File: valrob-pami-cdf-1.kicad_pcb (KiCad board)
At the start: 4 copper layers, 58 x 50 mm, 138 parts, among them J1 Conn_01x04, J2 USB_C_Receptacle_USB2.0_14P, J3 Conn_01x02, J4 Conn_01x04_Pin, J5 Conn_01x06, M1 Motor_Servo, M2 Stepper_Motor_bipolar, M3 Stepper_Motor_bipolar, Q1 Q_NMOS, Q2 Q_NMOS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

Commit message: pcb: add RGB led routing
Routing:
- net /RGB1: track 0.00 -> 14.3 mm
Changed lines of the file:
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@@
+	)
+	(segment
+		(start 162.25 98)
+		(end 161.5 98.75)
+		(width 0.2)
+		(layer "F.Cu")
+		(net 37)
+	)
+	(segment
+		(start 161.5 98.75)
+		(end 158 98.75)
+		(width 0.2)
+		(layer "F.Cu")
+		(net 37)
+	)
+	(segment
+		(start 162.25 94.75)
+		(end 162.25 98)
+		(width 0.2)
+		(layer "F.Cu")
+		(net 37)
+	)
+	(segment
+		(start 164.8 91.7)
+		(end 164.531 91.969)
+		(width 0.2)
+		(layer "F.Cu")
+		(net 37)
+	)
+	(segment
+		(start 158 98.75)
+		(end 157.6 98.35)
+		(width 0.2)
+		(layer "F.Cu")
+		(net 37)
+	)
+	(segment
+		(start 164.531 92.469)
+		(end 162.25 94.75)
+		(width 0.2)
+		(layer "F.Cu")
+		(net 37)
+	)
+	(segment
+		(start 165.3 91.7)
+		(end 164.8 91.7)
+		(width 0.2)
+		(layer "F.Cu")
+		(net 37)
+	)
+	(segment
+		(start 157.6 98.35)
+		(end 157.6 97.05)
+		(width 0.2)
+		(layer "F.Cu")
+		(net 37)
+	)
+	(segment
+		(start 164.531 91.969)
+		(end 164.531 92.469)
+		(width 0.2)
+		(layer "F.Cu")
+		(net 37)
 	)
 	(segment
@@
 	)
 	(segment
-		(start 165.3 91.3)
-		(end 164.872936 91.3)
+		(start 164.01 91.75)
+		(end 164.25 91.51)
 		(width 0.2)
 		(layer "F.Cu")
@@
 	)
 	(segment
-		(start 164.422936 91.75)
-		(end 164.01 91.75)
+		(start 164.25 91.5)
+		(end 164.45 91.3)
 		(width 0.2)
 		(layer "F.Cu")
@@
 	)
 	(segment
-		(start 164.872936 91.3)
-		(end 164.422936 91.75)
-		(width 0.2)
-		(layer "F.Cu")
+		(start 164.25 91.51)
+		(end 164.25 91.5)
+		(width 0.2)
+		(layer "F.Cu")
+		(net 78)
+	)
+	(segment
+		(start 164.45 91.3)
+		(end 165.3 91.3)
+		(width 0.2)
+		(layer "F.Cu")

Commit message: pcb: add spare gpio routing
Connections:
- U4 pad 39: Net-(J5-Pin_2) -> Net-(J5-Pin_4)
- U4 pad 40: Net-(J5-Pin_3) -> Net-(J5-Pin_2)
- U4 pad 41: Net-(J5-Pin_4) -> Net-(J5-Pin_5)
- U4 pad 42: Net-(J5-Pin_5) -> Net-(J5-Pin_3)
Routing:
- net Net-(J5-Pin_2): track 0.00 -> 11.5 mm
- net Net-(J5-Pin_4): track 0.00 -> 9.92 mm, vias 0 -> 1
- net Net-(J5-Pin_3): track 0.00 -> 7.77 mm
- net Net-(J5-Pin_5): track 0.00 -> 5.07 mm
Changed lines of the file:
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@@
 			(layers "F.Cu" "F.Mask" "F.Paste")
 			(roundrect_rratio 0.25)
-			(net 118 "Net-(J5-Pin_2)")
+			(net 117 "Net-(J5-Pin_4)")
 			(pinfunction "GPIO34")
 			(pintype "bidirectional")
@@
 			(layers "F.Cu" "F.Mask" "F.Paste")
 			(roundrect_rratio 0.25)
-			(net 119 "Net-(J5-Pin_3)")
+			(net 118 "Net-(J5-Pin_2)")
 			(pinfunction "GPIO35")
 			(pintype "bidirectional")
@@
 			(layers "F.Cu" "F.Mask" "F.Paste")
 			(roundrect_rratio 0.25)
-			(net 117 "Net-(J5-Pin_4)")
+			(net 116 "Net-(J5-Pin_5)")
 			(pinfunction "GPIO36")
 			(pintype "bidirectional")
@@
 			(layers "F.Cu" "F.Mask" "F.Paste")
 			(roundrect_rratio 0.25)
-			(net 116 "Net-(J5-Pin_5)")
+			(net 119 "Net-(J5-Pin_3)")
 			(pinfunction "GPIO37")
 			(pintype "bidirectional")
@@
 	)
 	(segment
+		(start 169 97.21)
+		(end 169 96.5)
+		(width 0.2)
+		(layer "F.Cu")
+		(net 116)
+	)
+	(segment
+		(start 170.95 94.55)
+		(end 170.95 92.95)
+		(width 0.2)
+		(layer "F.Cu")
+		(net 116)
+	)
+	(segment
+		(start 169 96.5)
+		(end 170.95 94.55)
+		(width 0.2)
+		(layer "F.Cu")
+		(net 116)
+	)
+	(segment
+		(start 170.138088 92.938088)
+		(end 170.15 92.95)
+		(width 0.2)
+		(layer "F.Cu")
+		(net 117)
+	)
+	(segment
+		(start 170.138088 92.301707)
+		(end 170.138088 92.938088)
+		(width 0.2)
+		(layer "F.Cu")
+		(net 117)
+	)
+	(via
+		(at 170.138088 92.301707)
+		(size 0.5)
+		(drill 0.3)
+		(layers "F.Cu" "B.Cu")
+		(net 117)
+	)
+	(segment
+		(start 168.25 96)
+		(end 168.75 96)
+		(width 0.2)
+		(layer "B.Cu")
+		(net 117)
+	)
+	(segment
+		(start 170.138088 94.611912)
+		(end 170.138088 92.301707)
+		(width 0.2)
+		(layer "B.Cu")
+		(net 117)
+	)
+	(segment
+		(start 167.75 98.46)
+		(end 167.75 96.5)
+		(width 0.2)
+		(layer "B.Cu")
+		(net 117)
+	)
+	(segment
+		(start 166.46 99.75)
+		(end 167.75 98.46)
+		(width 0.2)
+		(layer "B.Cu")
+		(net 117)
+	)
+	(segment
+		(start 167.75 96.5)
+		(end 168.25 96)
+		(width 0.2)
+		(layer "B.Cu")
+		(net 117)
+	)
+	(segment
+		(start 168.75 96)
+		(end 170.138088 94.611912)
+		(width 0.2)
+		(layer "B.Cu")
+		(net 117)
+	)
+	(segment
+		(start 169.003612 96)
+		(end 170.55 94.453612)
+		(width 0.2)
+		(layer "F.Cu")
+		(net 118)
+	)
+	(segment
+		(start 166.46 102.29)
+		(end 167.75 101)
+		(width 0.2)
+		(layer "F.Cu")
+		(net 118)
+	)
+	(segment
+		(start 170.55 94.453612)
+		(end 170.55 92.95)
+		(width 0.2)
+		(layer "F.Cu")
+		(net 118)
+	)
+	(segment
+		(start 167.75 101)
+		(end 167.75 96.543479)
+		(width 0.2)
+		(layer "F.Cu")
+		(net 118)
+	)
+	(segment
+		(start 167.75 96.543479)
+		(end 168.293479 96)
+		(width 0.2)
+		(layer "F.Cu")
+		(net 118)
+	)
+	(segment
+		(start 168.293479 96)
+		(end 169.003612 96)
+		(width 0.2)
+		(layer "F.Cu")
+		(net 118)
+	)
+	(segment
+		(start 171.35 94.65)
+		(end 171.35 92.95)
+		(width 0.2)
+		(layer "F.Cu")
+		(net 119)
+	)
+	(segment
+		(start 170.101 95.899)
+		(end 171.35 94.65)
+		(width 0.2)
+		(layer "F.Cu")
+		(net 119)
+	)
+	(segment
+		(start 169 99.75)
+		(end 170.101 98.649)
+		(width 0.2)
+		(layer "F.Cu")
+		(net 119)
+	)
+	(segment
+		(start 170.101 98.649)
+		(end 170.101 95.899)
+		(width 0.2)
+		(layer "F.Cu")
+		(net 119)
+	)
+	(segment

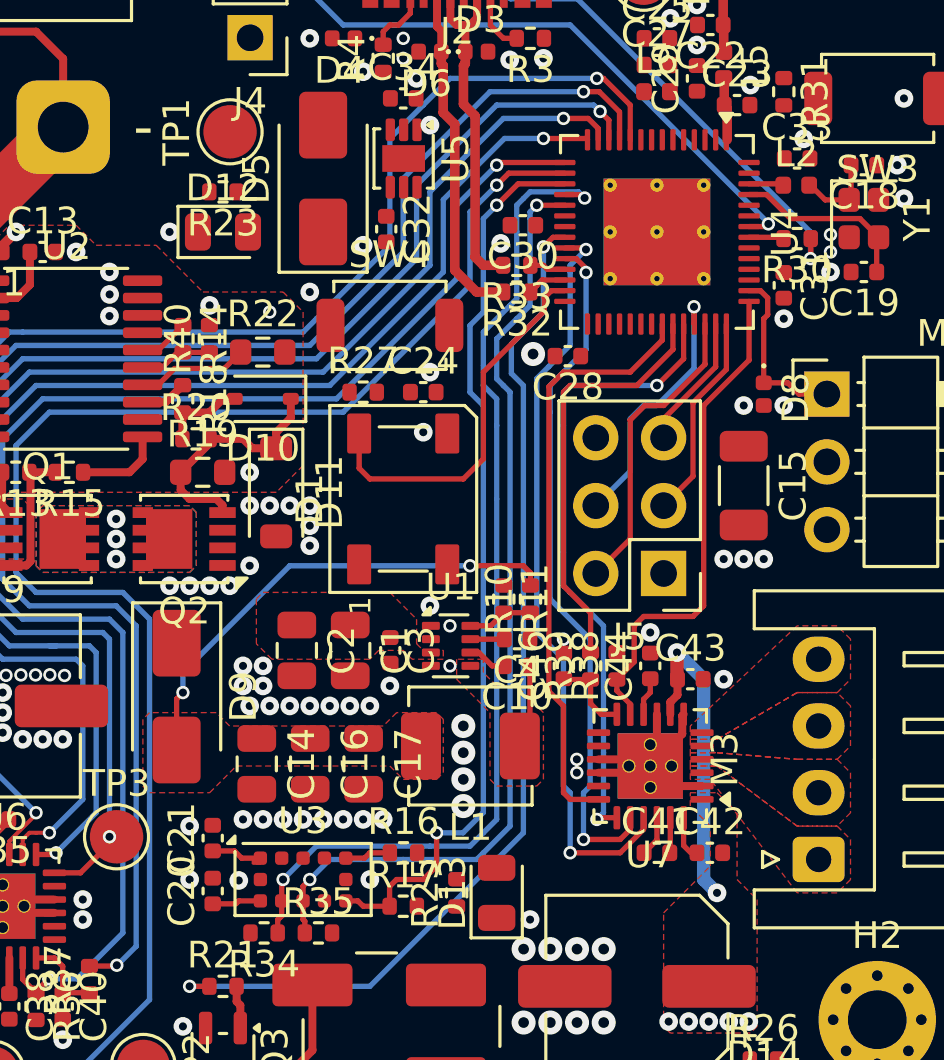
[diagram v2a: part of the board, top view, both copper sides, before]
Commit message: pcb: fix right stepper drv gnd island
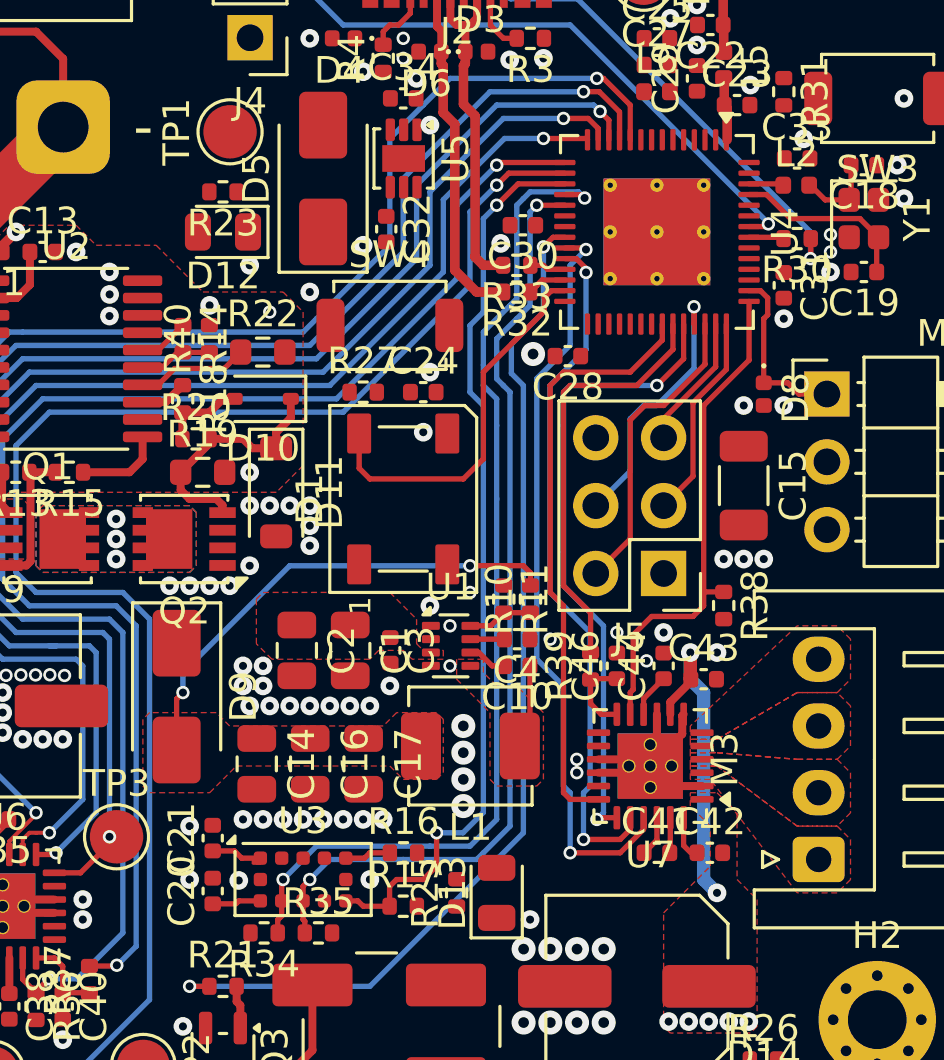
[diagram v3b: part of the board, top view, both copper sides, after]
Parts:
- moved R38 4.59 mm to (171.2, 103.5), turned to -90 degrees
- moved C46 1.99 mm to (167.2, 105.8)
- moved C43 0.50 mm to (170.5, 106.2)
- moved C44 0.50 mm to (169.0, 105.8)
- turned D12 to 180 degrees
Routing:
- net GND: vias 111 -> 114

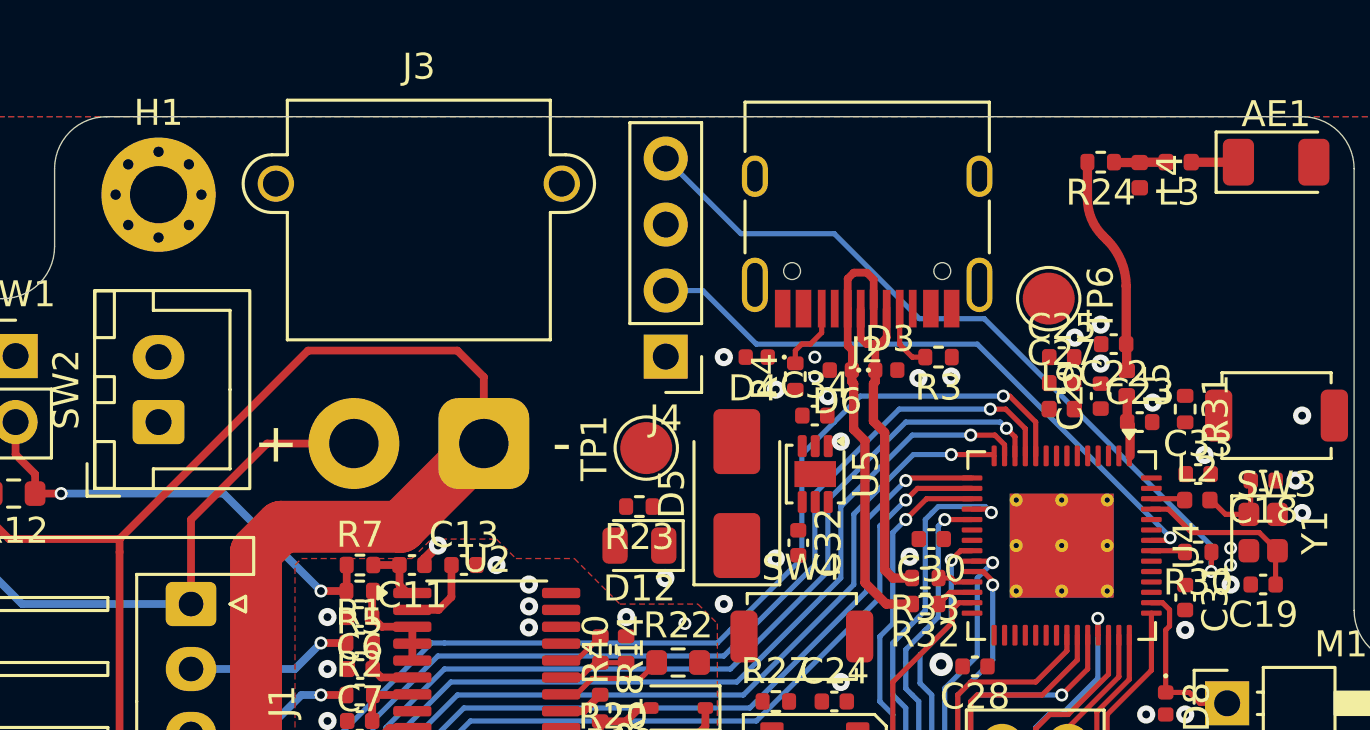
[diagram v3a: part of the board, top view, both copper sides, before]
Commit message: pcb: add EMS routing
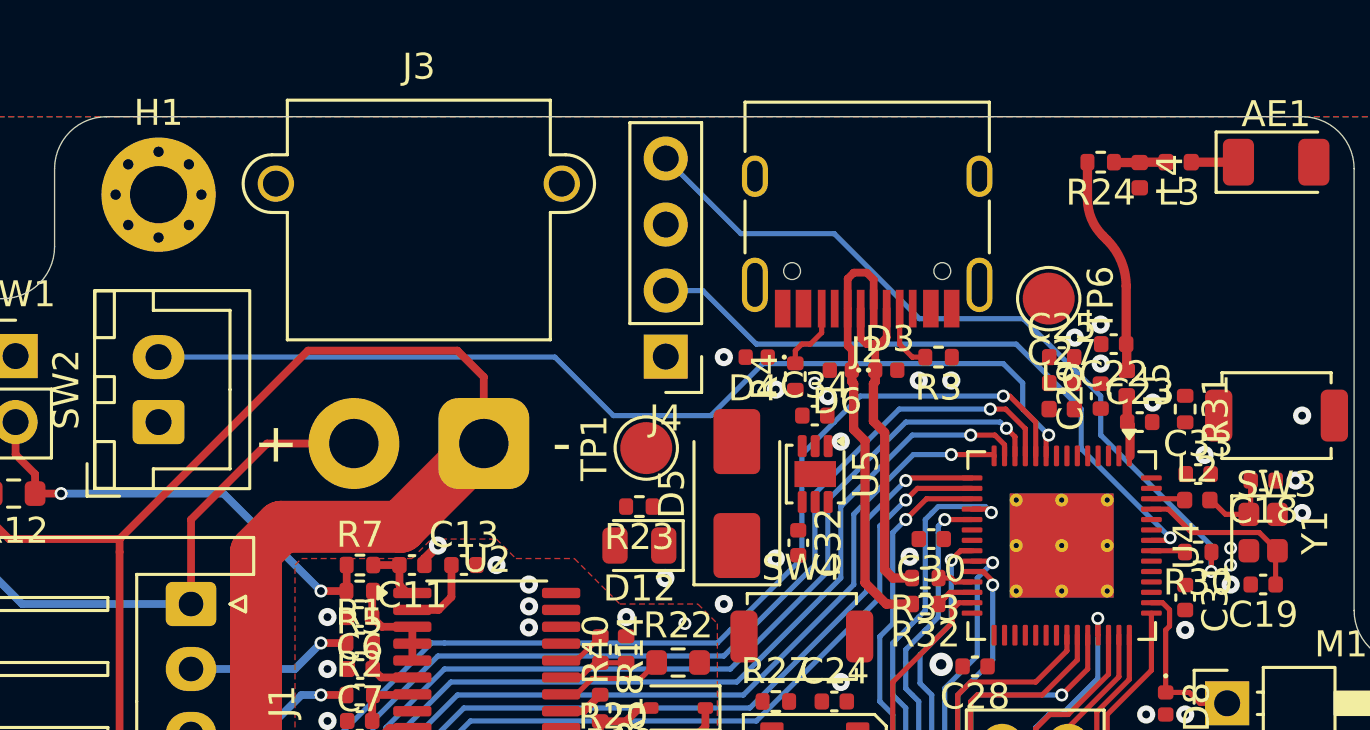
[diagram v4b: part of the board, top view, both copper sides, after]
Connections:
- U4 pad 7: /EMS -> unconnected-(U4-GPIO2/ADC1_CH1-Pad7)
- U4 pad 9: unconnected-(U4-GPIO4/ADC1_CH3-Pad9) -> /EMS
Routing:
- net /EMS: track 0.00 -> 38.6 mm, vias 0 -> 1
- net /U0RXD: track 24.1 -> 25.1 mm
- net Net-(J4-Pin_4): track 28.9 -> 29.8 mm
- net GND: vias 114 -> 113
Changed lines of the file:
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@@
 	(net 121 "unconnected-(U4-GPIO1{slash}ADC1_CH0-Pad6)")
 	(net 122 "unconnected-(U4-GPIO3{slash}ADC1_CH2-Pad8)")
-	(net 123 "unconnected-(U4-GPIO4{slash}ADC1_CH3-Pad9)")
+	(net 123 "unconnected-(U4-GPIO2{slash}ADC1_CH1-Pad7)")
 	(footprint "GLCS:Texas_RGE0024B_VQFN-24-1EP_4x4mm_P0.5mm_EP2.5x2.5mm_ThermalVias"
 		(layer "F.Cu")
@@
 			(layers "F.Cu" "F.Mask" "F.Paste")
 			(roundrect_rratio 0.25)
-			(net 86 "/EMS")
+			(net 123 "unconnected-(U4-GPIO2{slash}ADC1_CH1-Pad7)")
 			(pinfunction "GPIO2/ADC1_CH1")
 			(pintype "bidirectional")
@@
 			(layers "F.Cu" "F.Mask" "F.Paste")
 			(roundrect_rratio 0.25)
-			(net 123 "unconnected-(U4-GPIO4{slash}ADC1_CH3-Pad9)")
+			(net 86 "/EMS")
 			(pinfunction "GPIO4/ADC1_CH3")
 			(pintype "bidirectional")
@@
 	)
 	(via
-		(at 159.25 82.25)
-		(size 0.5)
-		(drill 0.3)
-		(layers "F.Cu" "B.Cu")
-		(free yes)
-		(net 4)
-	)
-	(via
 		(at 155.75 101.25)
 		(size 0.7)
@@
 	)
 	(via
-		(at 164.5 83)
+		(at 164.5 83.15)
 		(size 0.7)
 		(drill 0.3)
@@
 	)
 	(via
-		(at 163.236556 83.056892)
+		(at 163.25 83.15)
 		(size 0.7)
 		(drill 0.3)
@@
 	)
 	(via
-		(at 159.25 83)
+		(at 159.25 83.25)
 		(size 0.5)
 		(drill 0.3)
@@
 	)
 	(segment
+		(start 169.5 85.775835)
+		(end 169.5 84.25)
+		(width 0.2)
+		(layer "B.Cu")
+		(net 50)
+	)
+	(segment
 		(start 154.94 79.69)
 		(end 153.515 79.69)
@@
 	)
 	(segment
+		(start 169.5 84.25)
+		(end 167 81.75)
+		(width 0.2)
+		(layer "B.Cu")
+		(net 50)
+	)
+	(segment
 		(start 157 81.75)
 		(end 154.94 79.69)
@@
 	)
 	(segment
-		(start 172.924165 89.174165)
-		(end 165.5 81.75)
+		(start 172.924165 89.2)
+		(end 169.5 85.775835)
 		(width 0.2)
 		(layer "B.Cu")
@@
 	)
 	(segment
-		(start 165.5 81.75)
+		(start 167 81.75)
 		(end 157 81.75)
 		(width 0.2)
@@
 	)
 	(segment
-		(start 156.405 77.5)
-		(end 160 77.5)
+		(start 170.25 83.75)
+		(end 167.271 80.771)
 		(width 0.2)
 		(layer "B.Cu")
@@
 	(segment
 		(start 174.5 89.5)
-		(end 174.5 90.5)
+		(end 170.25 85.25)
 		(width 0.2)
 		(layer "B.Cu")
@@
 	)
 	(segment
-		(start 165.771 80.771)
+		(start 160 77.5)
+		(end 156.405 77.5)
+		(width 0.2)
+		(layer "B.Cu")
+		(net 51)
+	)
+	(segment
+		(start 174.5 90.5)
 		(end 174.5 89.5)
 		(width 0.2)
@@
 	)
 	(segment
-		(start 153.515 74.61)
-		(end 156.405 77.5)
+		(start 156.405 77.5)
+		(end 153.515 74.61)
 		(width 0.2)
 		(layer "B.Cu")
@@
 	(segment
 		(start 163.271 80.771)
-		(end 165.771 80.771)
+		(end 160 77.5)
 		(width 0.2)
 		(layer "B.Cu")
@@
 	)
 	(segment
-		(start 160 77.5)
+		(start 170.25 85.25)
+		(end 170.25 83.75)
+		(width 0.2)
+		(layer "B.Cu")
+		(net 51)
+	)
+	(segment
+		(start 167.271 80.771)
 		(end 163.271 80.771)
 		(width 0.2)
@@
 	)
 	(segment
+		(start 168.25 85.25)
+		(end 168.15 85.35)
+		(width 0.2)
+		(layer "F.Cu")
+		(net 86)
+	)
+	(segment
+		(start 168.15 85.35)
+		(end 168.15 86.05)
+		(width 0.2)
+		(layer "F.Cu")
+		(net 86)
+	)
+	(via
+		(at 168.25 85.25)
+		(size 0.5)
+		(drill 0.3)
+		(layers "F.Cu" "B.Cu")
+		(net 86)
+	)
+	(segment
+		(start 157.25 82.5)
+		(end 155.25 84.5)
+		(width 0.2)
+		(layer "B.Cu")
+		(net 86)
+	)
+	(segment
+		(start 168.25 85.25)
+		(end 167.25 84.25)
+		(width 0.2)
+		(layer "B.Cu")
+		(net 86)
+	)
+	(segment
+		(start 151.5 84.5)
+		(end 149.25 82.25)
+		(width 0.2)
+		(layer "B.Cu")
+		(net 86)
+	)
+	(segment
+		(start 167.25 84.25)
+		(end 167.25 83.25)
+		(width 0.2)
+		(layer "B.Cu")
+		(net 86)
+	)
+	(segment
+		(start 167.25 83.25)
+		(end 166.5 82.5)
+		(width 0.2)
+		(layer "B.Cu")
+		(net 86)
+	)
+	(segment
+		(start 149.25 82.25)
+		(end 134 82.25)
+		(width 0.2)
+		(layer "B.Cu")
+		(net 86)
+	)
+	(segment
+		(start 155.25 84.5)
+		(end 151.5 84.5)
+		(width 0.2)
+		(layer "B.Cu")
+		(net 86)
+	)
+	(segment
+		(start 166.5 82.5)
+		(end 157.25 82.5)
+		(width 0.2)
+		(layer "B.Cu")
+		(net 86)
+	)
+	(segment
